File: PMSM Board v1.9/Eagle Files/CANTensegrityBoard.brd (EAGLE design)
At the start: 82.5 x 48 mm, 127 parts, among them IC1 DRV8303, U2 SN65HVD232_D_8, U3 SN65LVDT348_PW_1, U6 DSPIC33EP256MU80, U7 TPS84250_RKG_41

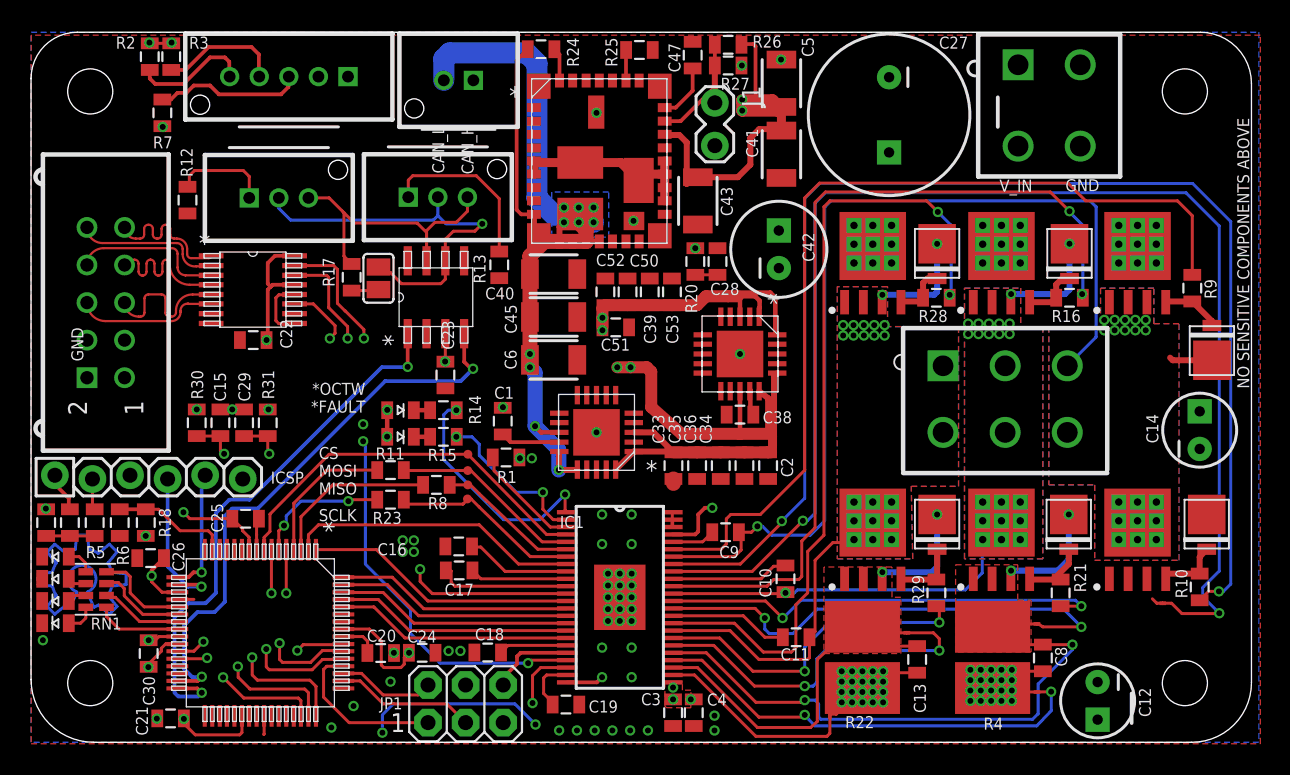
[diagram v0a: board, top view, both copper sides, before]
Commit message: Motor control work and board dimension corrections.
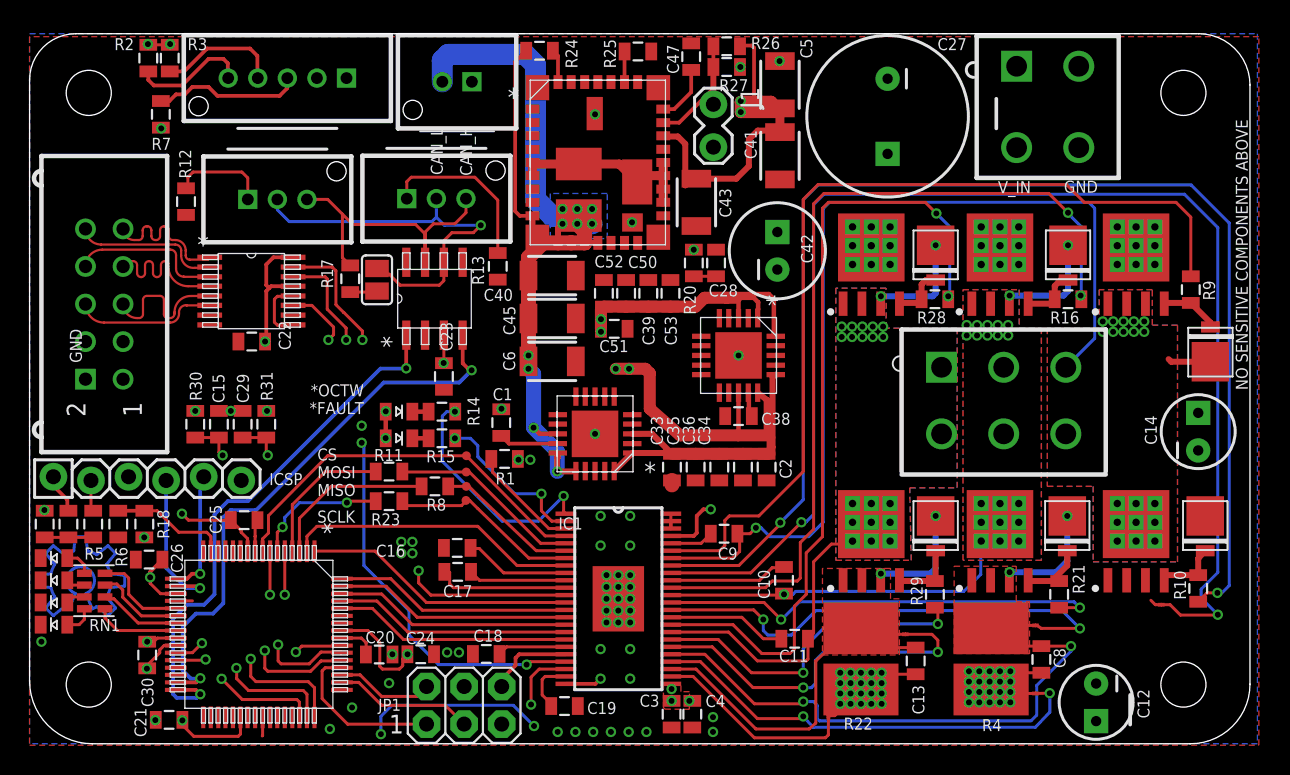
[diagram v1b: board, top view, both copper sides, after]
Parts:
- C15, C29: value (none) -> 10n
- R10, R16, R21, R28, R29, R9: value (none) -> 4.7
- R11, R23, R8: value (none) -> 150
- R2, R3, R7: value (none) -> 10k
- R30, R31: value (none) -> 15k
- moved U$17 0.14 mm to (65.8, 23.2)
- moved U$4 0.14 mm to (74.8, 32.4)
- moved U$5 0.14 mm to (65.6, 32.4)
- moved U$7 0.14 mm to (74.8, 13.7)
- moved U$8 0.14 mm to (65.6, 13.7)
- moved C12 0.14 mm to (72.1, 2.80)
- moved R21 0.14 mm to (69.6, 10.1)
- moved U$26 0.14 mm to (79.5, 15.4)
- moved C27 0.14 mm to (58.0, 42.4)
- moved C28 0.14 mm to (46.4, 32.5)
- moved C33 0.14 mm to (43.4, 18.7)
- moved C34 0.14 mm to (48.2, 18.7)
- moved C35 0.14 mm to (45.0, 18.7)
- moved C36 0.14 mm to (46.6, 18.7)
- moved C38 0.14 mm to (47.9, 22.1)
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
